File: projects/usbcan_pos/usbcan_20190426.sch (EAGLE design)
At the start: 45 parts, among them J1 8P8C-LED, J2 MICRO-USB-RECEPTACLE47589-0001, J3 MA04-1, J4 MA02-2, U1 STM32F302C, U2 NCV7351D1E, U3 SI8621AB-B-IS, U4 AP2127N-3.3TRG1, U5 78L05F, X1 CSTCE8M00G55

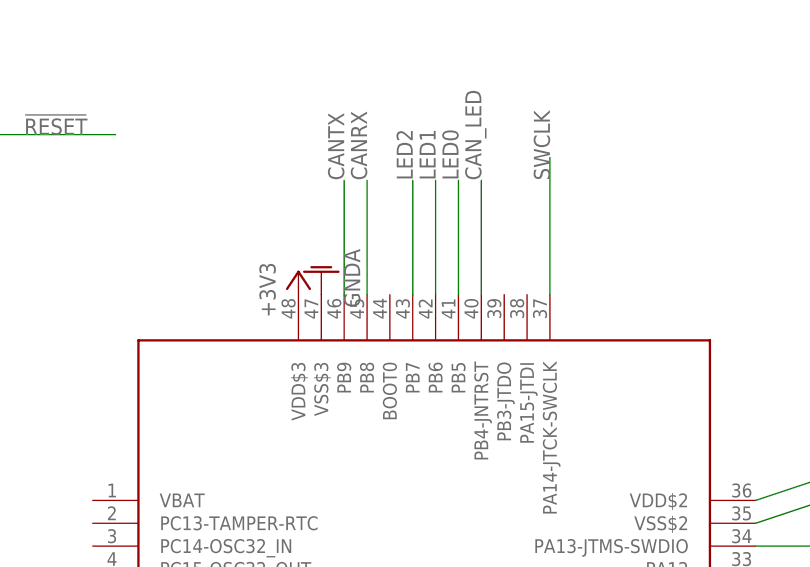
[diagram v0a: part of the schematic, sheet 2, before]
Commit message: usbcan 修正済み　BLDCMD完成
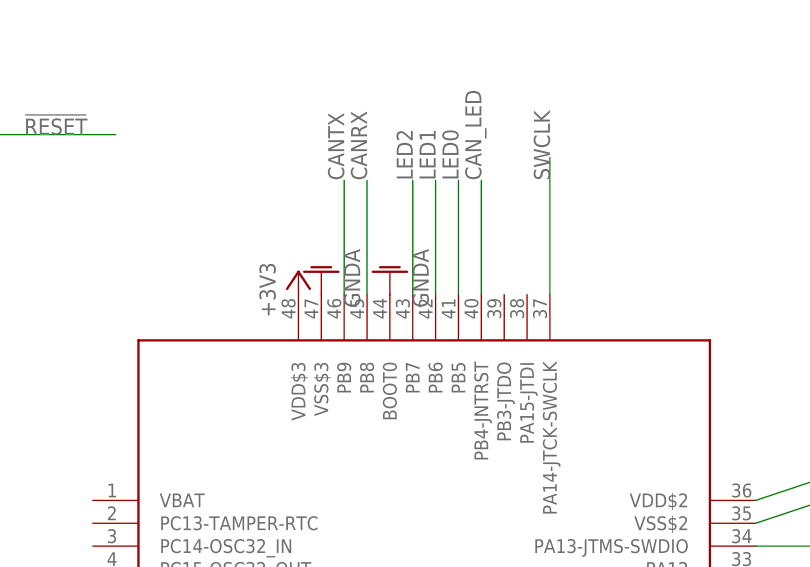
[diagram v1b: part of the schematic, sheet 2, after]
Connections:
- net GNDA: now also U1.BOOT0
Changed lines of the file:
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@@
 <?xml version="1.0" encoding="utf-8"?>
 <!DOCTYPE eagle SYSTEM "eagle.dtd">
-<eagle version="9.3.0">
+<eagle version="9.3.2">
 <drawing>
 <settings>
@@
 <part name="TP4" library="testpad" library_urn="urn:adsk.eagle:library:385" deviceset="TP" device="B1,27" package3d_urn="urn:adsk.eagle:package:27944/1"/>
 <part name="TP5" library="testpad" library_urn="urn:adsk.eagle:library:385" deviceset="TP" device="B1,27" package3d_urn="urn:adsk.eagle:package:27944/1"/>
+<part name="GND34" library="supply1" library_urn="urn:adsk.eagle:library:371" deviceset="GNDA" device=""/>
 </parts>
 <sheets>
@@
 <attribute name="NAME" x="229.87" y="21.59" size="1.778" layer="95" rot="R90"/>
 <attribute name="TP_SIGNAL_NAME" x="232.41" y="24.13" size="1.778" layer="97" rot="R90"/>
+</instance>
+<instance part="GND34" gate="1" x="50.8" y="96.52" smashed="yes" rot="R180">
+<attribute name="VALUE" x="53.34" y="99.06" size="1.778" layer="96" rot="R270"/>
 </instance>
 </instances>
@@
 <wire x1="195.58" y1="2.54" x2="195.58" y2="10.16" width="0.1524" layer="91"/>
 </segment>
-</net>
+<segment>
+<pinref part="U1" gate="G$1" pin="BOOT0"/>
+<pinref part="GND34" gate="1" pin="GNDA"/>
+</segment>
+</net>
